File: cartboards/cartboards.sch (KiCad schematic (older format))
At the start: 1 part

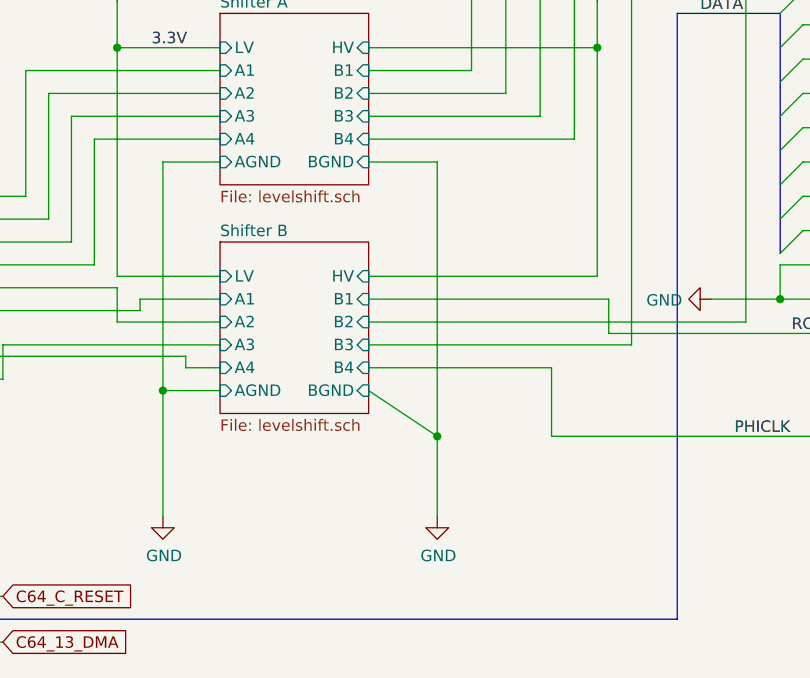
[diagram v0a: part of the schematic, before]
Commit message: Tweak trace width for power in schematics
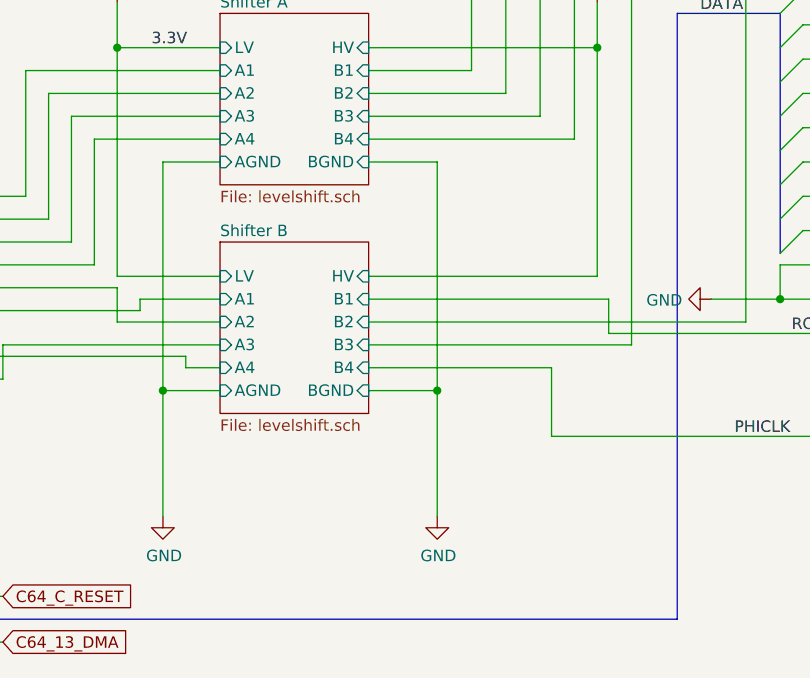
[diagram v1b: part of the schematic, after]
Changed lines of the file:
@@
 	7500 3700 7750 3700
 Wire Wire Line
-	8700 5250 8700 4900
-Wire Wire Line
 	8700 3700 8400 3700
-Wire Wire Line
-	8400 4700 8700 4900
-Connection ~ 8700 4900
-Wire Wire Line
-	8700 4900 8700 3700
 Wire Wire Line
 	3600 2850 3600 2750
@@
 Wire Wire Line
 	6350 4550 7600 4550
+Wire Wire Line
+	8400 4700 8700 4700
+Connection ~ 8700 4700
+Wire Wire Line
+	8700 4700 8700 3700
+Wire Wire Line
+	8700 4700 8700 5250
 Wire Bus Line
 	10200 3050 10200 4100
